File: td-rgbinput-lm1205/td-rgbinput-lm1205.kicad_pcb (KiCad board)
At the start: 2 copper layers, 100 x 50 mm, 68 parts, among them J1 Conn_01x10_Socket, J16 Conn_01x06_Male, J17 Conn_01x06_Male, J2 Conn_01x07_Male, J3 Conn_01x05_Pin, J4 Conn_01x06_Male, J5 DB15_Female_HighDensity, U1 AP2205-33W5-7, U11 24LC08, U18 LM1205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

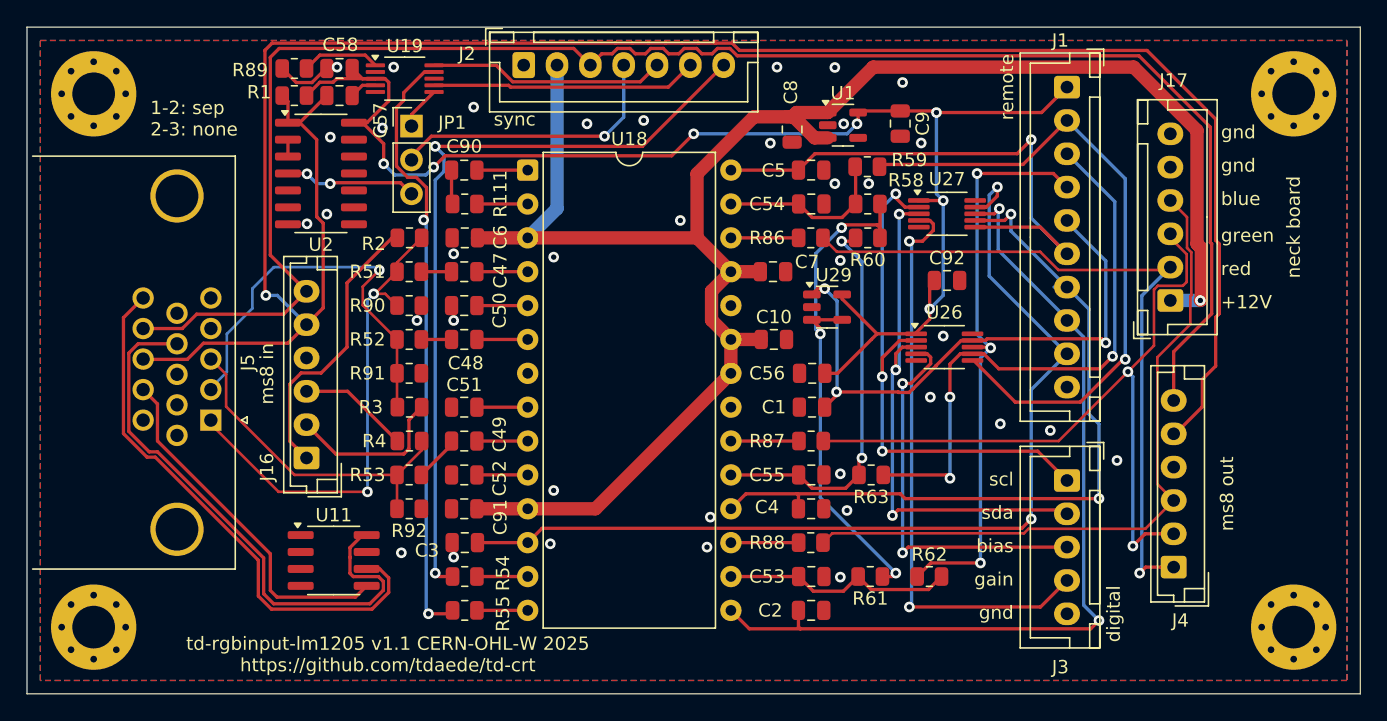
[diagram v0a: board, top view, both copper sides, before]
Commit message: Update td-rgbinput-lm1205 to add a linear regulator.
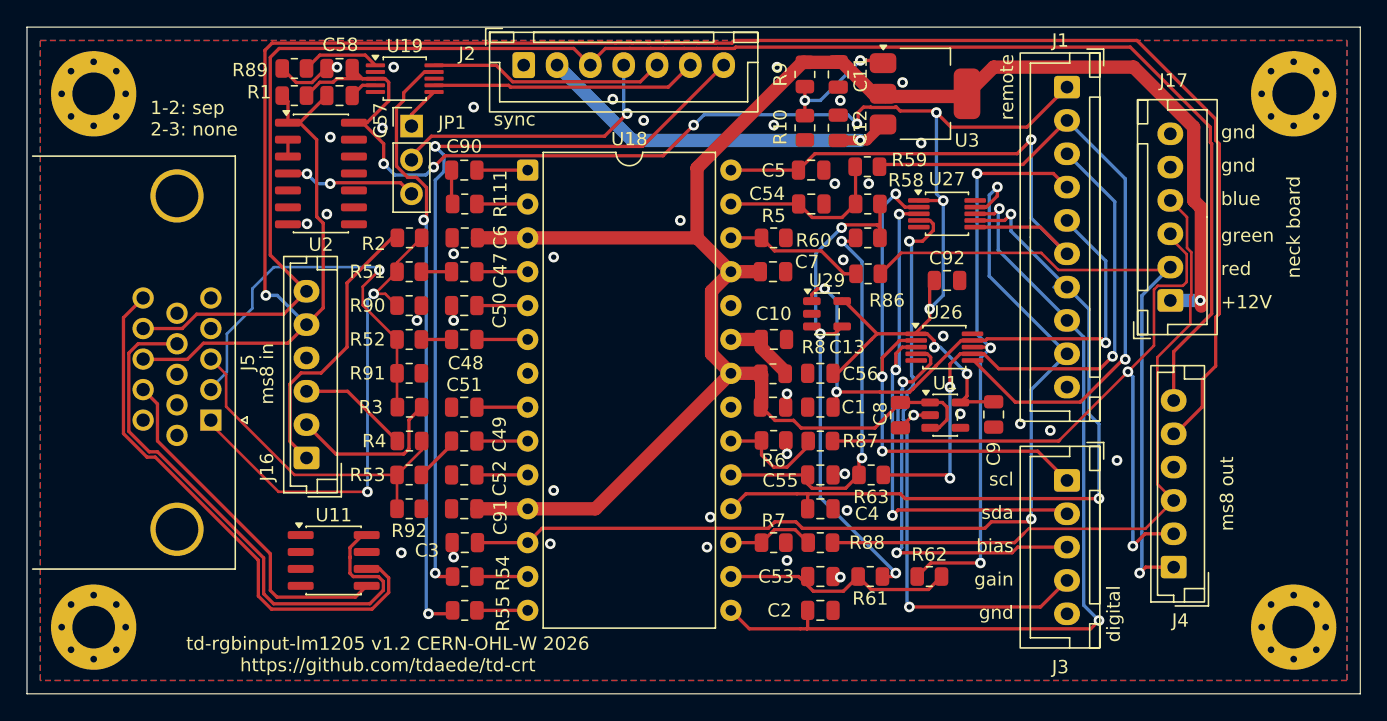
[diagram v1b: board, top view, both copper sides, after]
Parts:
- added C11: 10uF, Capacitor_SMD:C_0805_2012Metric, F.Cu at (132.8, 54.5)
- added C12: 10uF, Capacitor_SMD:C_0805_2012Metric, F.Cu at (132.8, 58.5)
- added C13: 10uF, Capacitor_SMD:C_0805_2012Metric, F.Cu at (128.0, 79.5)
- added R10: 2.2k, Resistor_SMD:R_0805_2012Metric, F.Cu at (130.3, 58.5)
- added R5: 390, Resistor_SMD:R_0805_2012Metric, F.Cu at (128.0, 66.8)
- added R6: 390, Resistor_SMD:R_0805_2012Metric, F.Cu at (128.0, 82.0)
- added R7: 390, Resistor_SMD:R_0805_2012Metric, F.Cu at (128.0, 89.7)
- added R8: 10, Resistor_SMD:R_0805_2012Metric, F.Cu at (128.0, 77.0)
- added R9: 280, Resistor_SMD:R_0805_2012Metric, F.Cu at (130.3, 54.5)
- added U3: AZ1117-ADJ, Package_TO_SOT_SMD:SOT-223-3_TabPin2, F.Cu at (139.3, 56.0)
- C10: value 1uF -> 10uF
- moved U1 23.1 mm to (140.9, 80.1)
- moved C9 22.9 mm to (144.5, 80.0)
- moved C8 22.9 mm to (137.5, 80.1)
- moved R86 5.08 mm to (135.1, 69.5)
- moved R88 0.71 mm to (131.5, 89.7)
- moved C2 0.69 mm to (131.5, 94.7)
- moved C4 0.69 mm to (131.5, 87.1)
- moved R87 0.69 mm to (131.5, 82.0)
- moved C53 0.68 mm to (131.5, 92.2)
- moved C55 0.68 mm to (131.5, 84.6)
- moved C1 0.62 mm to (131.5, 79.5)
- moved C56 0.61 mm to (131.5, 77.0)
- moved U29 0.50 mm to (132.0, 72.5)
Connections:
- C10 pad 1: +12V -> Net-(C10-Pad1)
- C6 pad 1: +12V -> +12VA
- C7 pad 1: +12V -> +12VA
- C8 pad 1: +12V -> +12VA
- C91 pad 1: +12V -> +12VA
- J17 pad 1: +12V -> +12VA
- U1 pad 1: +12V -> +12VA
- U1 pad 3: +12V -> +12VA
- U18 pad 11: +12V -> +12VA
- U18 pad 22: +12V -> +12VA
- U18 pad 23: +12V -> Net-(C10-Pad1)
- U18 pad 25: +12V -> +12VA
- U18 pad 3: +12V -> +12VA
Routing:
- net +12VA: track 0.00 -> 143.6 mm, vias 0 -> 1
- net +12V: track 136.8 -> 28.9 mm
- net +3.3V: track 106.7 -> 117.3 mm, vias 7 -> 9
- net Net-(U3-ADJ): track 0.00 -> 9.36 mm, vias 0 -> 2
- net Net-(C10-Pad1): track 0.00 -> 5.60 mm
- net Net-(U18-RED_VIDEO_OUT): track 5.08 -> 10.5 mm
- net r_yoke: track 53.8 -> 49.7 mm
- net Net-(U18-GREEN_VIDEO_OUT): track 5.11 -> 8.31 mm
- net GND: track 4.22 -> 6.84 mm, vias 37 -> 40
- net /rgb/globalbias_amp: track 39.5 -> 37.8 mm
- net Net-(U18-BLUE_VIDEO_OUT): track 5.08 -> 6.60 mm
- net BIAS_LOAD: track 29.6 -> 30.5 mm
- net vga_vsync: track 129.1 -> 128.2 mm
- net b_yoke: track 52.3 -> 51.6 mm
- net g_yoke: track 55.4 -> 54.9 mm
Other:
- board text added: "td-rgbinput-lm1205 v1.2 CERN-OHL-W 2026 https://github.com/tdaede/td-crt"
- board text removed: "td-rgbinput-lm1205 v1.1 CERN-OHL-W 2025 https://github.com/tdaede/td-crt"
